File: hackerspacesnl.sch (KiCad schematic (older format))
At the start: 44 parts

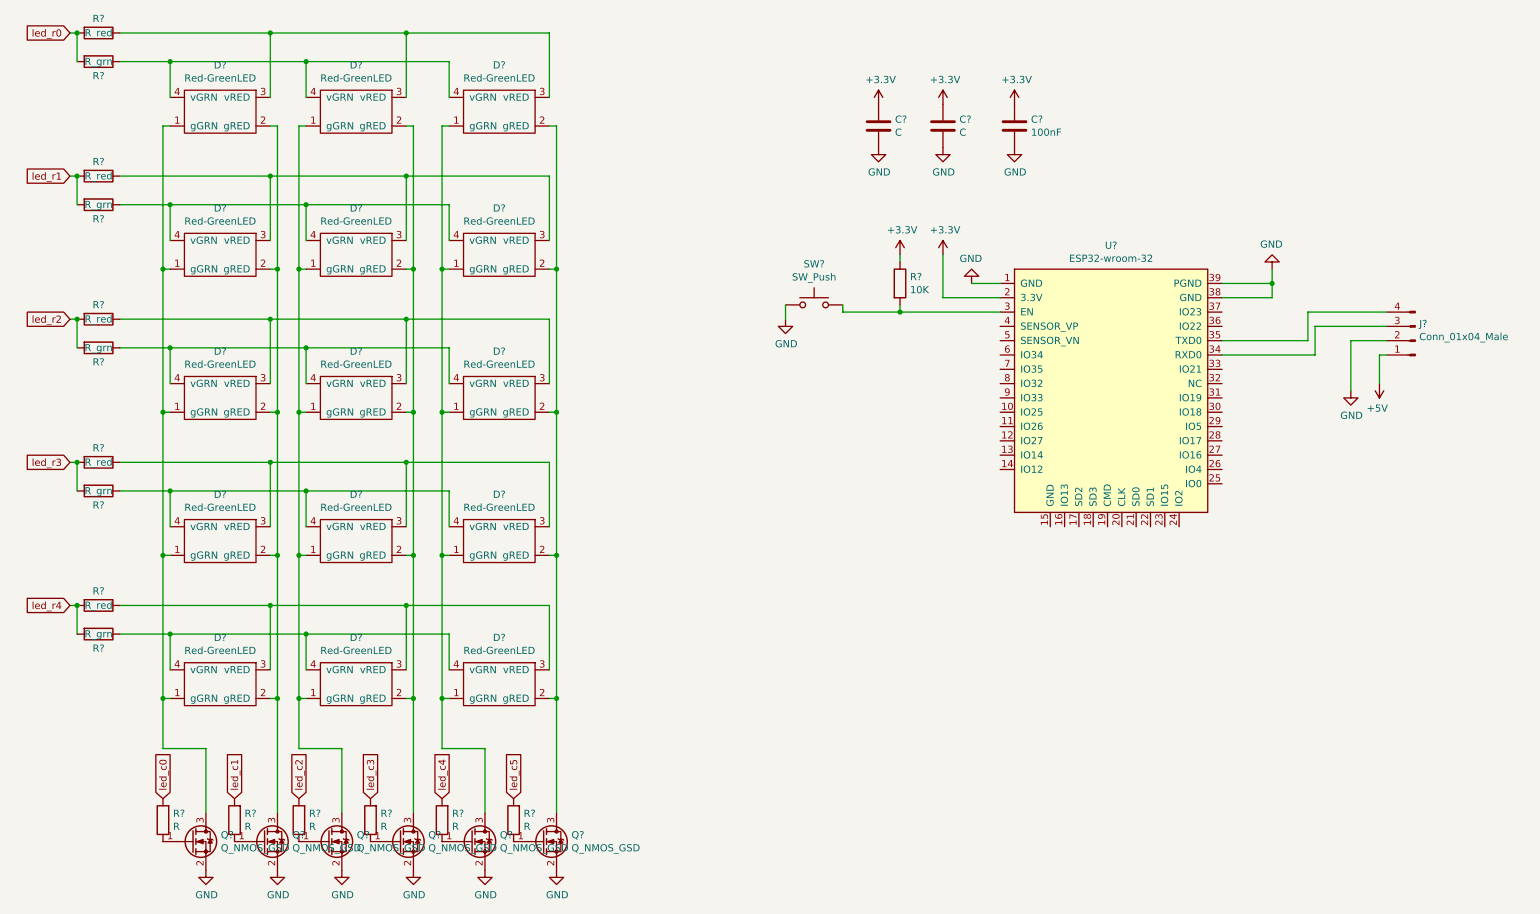
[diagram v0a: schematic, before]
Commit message: add values, connect matrix
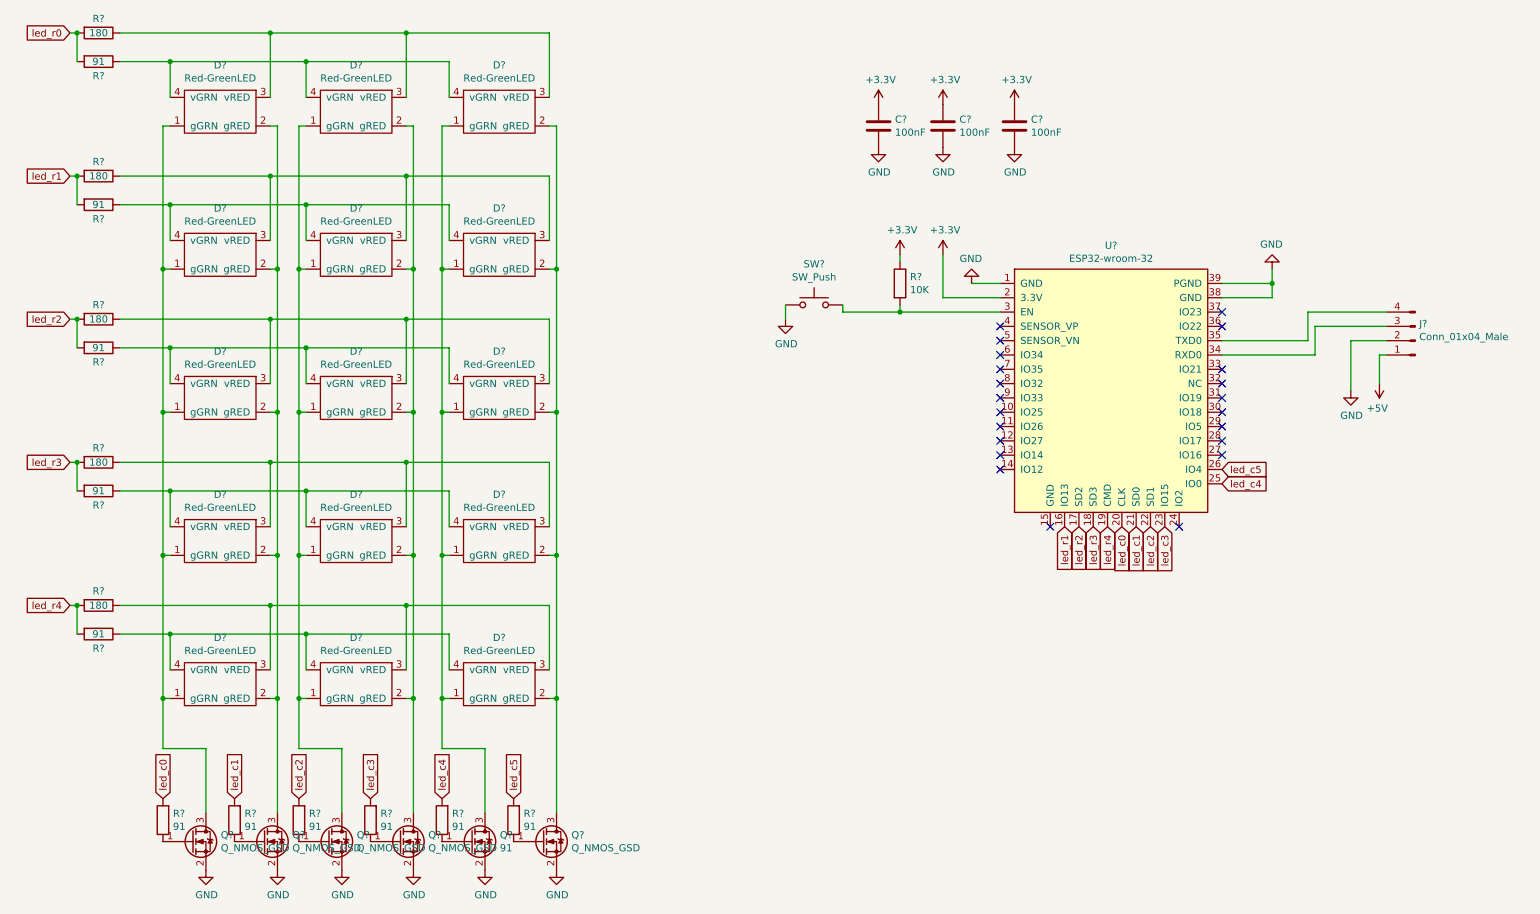
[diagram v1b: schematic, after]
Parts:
- C? (x2): value C -> 100nF
- Q?: value Q_NMOS_GSD -> 91
- R? (x5): value R_red -> 180
- R? (x5): value R_grn -> 91
- R? (x6): value R -> 91
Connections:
- net led_c0: now also U?.20 (CLK)
- net led_c1: now also U?.21 (SD0)
- net led_c2: now also U?.22 (SD1)
- net led_c3: now also U?.23 (IO15)
- net led_c4: now also U?.25 (IO0)
- net led_c5: now also U?.26 (IO4)
- net led_r1: now also U?.16 (IO13)
- net led_r2: now also U?.17 (SD2)
- net led_r3: now also U?.18 (SD3)
- net led_r4: now also U?.19 (CMD)
- no-connect marks 0 -> 22
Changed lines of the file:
@@
 P 1050 800
 F 0 "R?" V 950 800 50  0000 C CNN
-F 1 "R_red" V 1050 800 50  0000 C CNN
+F 1 "180" V 1050 800 50  0000 C CNN
 F 2 "" V 980 800 50  0001 C CNN
 F 3 "~" H 1050 800 50  0001 C CNN
@@
 P 3650 6450
 F 0 "Q?" H 3854 6496 50  0000 L CNN
-F 1 "Q_NMOS_GSD" H 3854 6405 50  0000 L CNN
+F 1 "91" H 3854 6405 50  0000 L CNN
 F 2 "" H 3850 6550 50  0001 C CNN
 F 3 "~" H 3650 6450 50  0001 C CNN
@@
 P 2000 6300
 F 0 "R?" H 1930 6254 50  0000 R CNN
-F 1 "R" H 1930 6345 50  0000 R CNN
+F 1 "91" H 1930 6345 50  0000 R CNN
 F 2 "" V 1930 6300 50  0001 C CNN
 F 3 "~" H 2000 6300 50  0001 C CNN
@@
 P 2450 6300
 F 0 "R?" H 2380 6254 50  0000 R CNN
-F 1 "R" H 2380 6345 50  0000 R CNN
+F 1 "91" H 2380 6345 50  0000 R CNN
 F 2 "" V 2380 6300 50  0001 C CNN
 F 3 "~" H 2450 6300 50  0001 C CNN
@@
 P 2950 6300
 F 0 "R?" H 2880 6254 50  0000 R CNN
-F 1 "R" H 2880 6345 50  0000 R CNN
+F 1 "91" H 2880 6345 50  0000 R CNN
 F 2 "" V 2880 6300 50  0001 C CNN
 F 3 "~" H 2950 6300 50  0001 C CNN
@@
 P 3450 6300
 F 0 "R?" H 3380 6254 50  0000 R CNN
-F 1 "R" H 3380 6345 50  0000 R CNN
+F 1 "91" H 3380 6345 50  0000 R CNN
 F 2 "" V 3380 6300 50  0001 C CNN
 F 3 "~" H 3450 6300 50  0001 C CNN
@@
 P 3950 6300
 F 0 "R?" H 3880 6254 50  0000 R CNN
-F 1 "R" H 3880 6345 50  0000 R CNN
+F 1 "91" H 3880 6345 50  0000 R CNN
 F 2 "" V 3880 6300 50  0001 C CNN
 F 3 "~" H 3950 6300 50  0001 C CNN
@@
 P 1500 6300
 F 0 "R?" H 1430 6254 50  0000 R CNN
-F 1 "R" H 1430 6345 50  0000 R CNN
+F 1 "91" H 1430 6345 50  0000 R CNN
 F 2 "" V 1430 6300 50  0001 C CNN
 F 3 "~" H 1500 6300 50  0001 C CNN
@@
 P 1050 1000
 F 0 "R?" V 1150 1000 50  0000 C CNN
-F 1 "R_grn" V 1050 1000 50  0000 C CNN
+F 1 "91" V 1050 1000 50  0000 C CNN
 F 2 "" V 980 1000 50  0001 C CNN
 F 3 "~" H 1050 1000 50  0001 C CNN
@@
 P 1050 2000
 F 0 "R?" V 1150 2000 50  0000 C CNN
-F 1 "R_grn" V 1050 2000 50  0000 C CNN
+F 1 "91" V 1050 2000 50  0000 C CNN
 F 2 "" V 980 2000 50  0001 C CNN
 F 3 "~" H 1050 2000 50  0001 C CNN
@@
 P 1050 1800
 F 0 "R?" V 950 1800 50  0000 C CNN
-F 1 "R_red" V 1050 1800 50  0000 C CNN
+F 1 "180" V 1050 1800 50  0000 C CNN
 F 2 "" V 980 1800 50  0001 C CNN
 F 3 "~" H 1050 1800 50  0001 C CNN
@@
 P 1050 3000
 F 0 "R?" V 1150 3000 50  0000 C CNN
-F 1 "R_grn" V 1050 3000 50  0000 C CNN
+F 1 "91" V 1050 3000 50  0000 C CNN
 F 2 "" V 980 3000 50  0001 C CNN
 F 3 "~" H 1050 3000 50  0001 C CNN
@@
 P 1050 2800
 F 0 "R?" V 950 2800 50  0000 C CNN
-F 1 "R_red" V 1050 2800 50  0000 C CNN
+F 1 "180" V 1050 2800 50  0000 C CNN
 F 2 "" V 980 2800 50  0001 C CNN
 F 3 "~" H 1050 2800 50  0001 C CNN
@@
 P 1050 4000
 F 0 "R?" V 1150 4000 50  0000 C CNN
-F 1 "R_grn" V 1050 4000 50  0000 C CNN
+F 1 "91" V 1050 4000 50  0000 C CNN
 F 2 "" V 980 4000 50  0001 C CNN
 F 3 "~" H 1050 4000 50  0001 C CNN
@@
 P 1050 3800
 F 0 "R?" V 950 3800 50  0000 C CNN
-F 1 "R_red" V 1050 3800 50  0000 C CNN
+F 1 "180" V 1050 3800 50  0000 C CNN
 F 2 "" V 980 3800 50  0001 C CNN
 F 3 "~" H 1050 3800 50  0001 C CNN
@@
 P 1050 5000
 F 0 "R?" V 1150 5000 50  0000 C CNN
-F 1 "R_grn" V 1050 5000 50  0000 C CNN
+F 1 "91" V 1050 5000 50  0000 C CNN
 F 2 "" V 980 5000 50  0001 C CNN
 F 3 "~" H 1050 5000 50  0001 C CNN
@@
 P 1050 4800
 F 0 "R?" V 950 4800 50  0000 C CNN
-F 1 "R_red" V 1050 4800 50  0000 C CNN
+F 1 "180" V 1050 4800 50  0000 C CNN
 F 2 "" V 980 4800 50  0001 C CNN
 F 3 "~" H 1050 4800 50  0001 C CNN
@@
 P 6500 1450
 F 0 "C?" H 6615 1496 50  0000 L CNN
-F 1 "C" H 6615 1405 50  0000 L CNN
+F 1 "100nF" H 6615 1405 50  0000 L CNN
 F 2 "" H 6538 1300 50  0001 C CNN
 F 3 "~" H 6500 1450 50  0001 C CNN
@@
 P 6950 1450
 F 0 "C?" H 7065 1496 50  0000 L CNN
-F 1 "C" H 7065 1405 50  0000 L CNN
+F 1 "100nF" H 7065 1405 50  0000 L CNN
 F 2 "" H 6988 1300 50  0001 C CNN
 F 3 "~" H 6950 1450 50  0001 C CNN
@@
 	1    0    0    -1
 $EndComp
+Text GLabel 7800 4250 3    50   Input ~ 0
+led_r1
+Text GLabel 7900 4250 3    50   Input ~ 0
+led_r2
+Text GLabel 8000 4250 3    50   Input ~ 0
+led_r3
+Text GLabel 8100 4250 3    50   Input ~ 0
+led_r4
+Text GLabel 8200 4250 3    50   Input ~ 0
+led_c0
+Text GLabel 8300 4250 3    50   Input ~ 0
+led_c1
+Text GLabel 8400 4250 3    50   Input ~ 0
+led_c2
+Text GLabel 8500 4250 3    50   Input ~ 0
+led_c3
+Text GLabel 8900 3950 2    50   Input ~ 0
+led_c4
+Text GLabel 8900 3850 2    50   Input ~ 0
+led_c5
+NoConn ~ 8600 4250
+NoConn ~ 7700 4250
+NoConn ~ 7350 3850
+NoConn ~ 7350 3750
+NoConn ~ 7350 3650
+NoConn ~ 7350 3550
+NoConn ~ 7350 3450
+NoConn ~ 7350 3350
+NoConn ~ 7350 3250
+NoConn ~ 7350 3150
+NoConn ~ 7350 3050
+NoConn ~ 7350 2950
+NoConn ~ 7350 2850
+NoConn ~ 8900 2750
+NoConn ~ 8900 2850
+NoConn ~ 8900 3150
+NoConn ~ 8900 3250
+NoConn ~ 8900 3350
+NoConn ~ 8900 3450
+NoConn ~ 8900 3550
+NoConn ~ 8900 3650
+NoConn ~ 8900 3750
 $EndSCHEMATC

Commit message: schema compleet
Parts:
- added C1: 10uF, Capacitor_SMD:C_0603_1608Metric, symbol Device:C
- added C2, C3: 100nF, Capacitor_SMD:C_0603_1608Metric, symbol Device:C
- added C6: 47uF, Capacitor_SMD:C_0805_2012Metric, symbol Device:C
- added J1: Screw_Terminal_01x02, Connector_Phoenix_MSTB:PhoenixContact_MSTBA_2,5_2-G-5,08_1x02_P5.08mm_Horizontal, symbol Connector:Screw_Terminal_01x02
- added R18: 10K, Resistor_SMD:R_0603_1608Metric, symbol Device:R
- added SW2: SW_Push, Button_Switch_SMD:SW_SPST_TL3342, symbol Switch:SW_Push
- added U1: AMS1117-3.3, Package_TO_SOT_SMD:SOT-223-3_TabPin2, symbol Regulator_Linear:AMS1117-3.3
- C4, C5: renamed from C?; footprint (none) -> Capacitor_SMD:C_0603_1608Metric
- J2: renamed from J?; footprint (none) -> Connector_PinHeader_2.54mm:PinHeader_1x04_P2.54mm_Vertical
- Q1, Q2, Q3, Q4, Q6: renamed from Q?; footprint (none) -> Package_TO_SOT_SMD:SOT-23
- Q5: renamed from Q?; value 91 -> Q_NMOS_GSD; footprint (none) -> Package_TO_SOT_SMD:SOT-23
- R1, R10, R11, R12, R13, R14, R15, R16, R2, R3, R4, R5, R6, R7, R8, R9: renamed from R?; footprint (none) -> Resistor_SMD:R_0603_1608Metric
- SW1: renamed from SW?; footprint (none) -> Button_Switch_SMD:SW_SPST_TL3342
- U2: renamed from U?; footprint (none) -> RF_Module:ESP32-WROOM-32
- gave numbers to parts that had none: 17
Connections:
- net +3V3: now also C3.1, C6.1, R18.1, U1.2 (VO)
- net +5V: now also C1.1, C2.1, J1.1 (Pin_1), U1.3 (VI)
- net GND: now also C1.2, C2.2, C3.2, C6.2, J1.2 (Pin_2), SW2.2, U1.1 (GND)
- net led_c0: now also U2.36 (IO22); no longer U2.20 (CLK)
- net led_c1: now also U2.33 (IO21); no longer U2.21 (SD0)
- net led_c2: now also U2.31 (IO19); no longer U2.22 (SD1)
- net led_c3: now also U2.30 (IO18); no longer U2.23 (IO15)
- net led_c4: now also U2.29 (IO5); no longer U2.25 (IO0)
- net led_c5: now also U2.28 (IO17); no longer U2.26 (IO4)
- net led_r1: now also U2.7 (IO35); no longer U2.16 (IO13)
- net led_r2: now also U2.8 (IO32); no longer U2.17 (SD2)
- net led_r3: now also U2.9 (IO33); no longer U2.18 (SD3)
- net led_r4: now also U2.10 (IO25); no longer U2.19 (CMD)
- new net: R18.2, SW2.1, U2.25 (IO0)
- no-connect marks 22 -> 3

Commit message: schemafoutje gefixt en eerste pcb stapjes
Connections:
- net led_r0: now also U2.14 (IO12)
- net led_r1: now also U2.16 (IO13); no longer U2.7 (IO35)
- net led_r2: now also U2.23 (IO15); no longer U2.8 (IO32)
- net led_r3: now also U2.24 (IO2); no longer U2.9 (IO33)
- net led_r4: now also U2.26 (IO4); no longer U2.10 (IO25)
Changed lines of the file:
@@
 	1    0    0    -1
 $EndComp
-Text GLabel 7150 3150 0    50   Input ~ 0
+Text GLabel 7800 4400 3    50   Input ~ 0
 led_r1
-Text GLabel 7150 3250 0    50   Input ~ 0
+Text GLabel 8500 4400 3    50   Input ~ 0
 led_r2
-Text GLabel 7150 3350 0    50   Input ~ 0
+Text GLabel 8600 4400 3    50   Input ~ 0
 led_r3
-Text GLabel 7150 3450 0    50   Input ~ 0
+Text GLabel 9100 3850 2    50   Input ~ 0
 led_r4
 Text GLabel 9100 2850 2    50   Input ~ 0
@@
 	9600 3500 9600 3550
 Wire Wire Line
-	7150 3150 7350 3150
-Wire Wire Line
-	7350 3250 7150 3250
-Wire Wire Line
-	7150 3350 7350 3350
-Wire Wire Line
-	7350 3450 7150 3450
-Wire Wire Line
 	9100 2850 8900 2850
 Wire Wire Line
@@
 Wire Wire Line
 	8900 3650 9100 3650
+Wire Wire Line
+	9100 3850 8900 3850
+Wire Wire Line
+	8600 4400 8600 4250
+Wire Wire Line
+	8500 4400 8500 4250
+Wire Wire Line
+	7800 4400 7800 4250
+Text GLabel 7200 3850 0    50   Input ~ 0
+led_r0
+Wire Wire Line
+	7200 3850 7350 3850
 $EndSCHEMATC

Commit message: led footprint
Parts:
- D1, D10, D11, D12, D13, D14, D15, D2, D3, D4, D5, D6, D7, D8, D9: footprint (none) -> hsnl:LED_0805_multicolor
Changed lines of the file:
@@
 F 0 "D1" V 1575 1350 50  0000 C CNN
 F 1 "Red-GreenLED" V 1666 1350 50  0000 C CNN
-F 2 "" V 1550 1500 50  0001 C CNN
+F 2 "hsnl:LED_0805_multicolor" V 1550 1500 50  0001 C CNN
 F 3 "" V 1550 1500 50  0001 C CNN
 	1    1900 1350
@@
 F 0 "D2" V 1575 2350 50  0000 C CNN
 F 1 "Red-GreenLED" V 1666 2350 50  0000 C CNN
-F 2 "" V 1550 2500 50  0001 C CNN
+F 2 "hsnl:LED_0805_multicolor" V 1550 2500 50  0001 C CNN
 F 3 "" V 1550 2500 50  0001 C CNN
 	1    1900 2350
@@
 F 0 "D3" V 1575 3350 50  0000 C CNN
 F 1 "Red-GreenLED" V 1666 3350 50  0000 C CNN
-F 2 "" V 1550 3500 50  0001 C CNN
+F 2 "hsnl:LED_0805_multicolor" V 1550 3500 50  0001 C CNN
 F 3 "" V 1550 3500 50  0001 C CNN
 	1    1900 3350
@@
 F 0 "D6" V 2525 1350 50  0000 C CNN
 F 1 "Red-GreenLED" V 2616 1350 50  0000 C CNN
-F 2 "" V 2500 1500 50  0001 C CNN
+F 2 "hsnl:LED_0805_multicolor" V 2500 1500 50  0001 C CNN
 F 3 "" V 2500 1500 50  0001 C CNN
 	1    2850 1350
@@
 F 0 "D7" V 2525 2350 50  0000 C CNN
 F 1 "Red-GreenLED" V 2616 2350 50  0000 C CNN
-F 2 "" V 2500 2500 50  0001 C CNN
+F 2 "hsnl:LED_0805_multicolor" V 2500 2500 50  0001 C CNN
 F 3 "" V 2500 2500 50  0001 C CNN
 	1    2850 2350
@@
 F 0 "D8" V 2525 3350 50  0000 C CNN
 F 1 "Red-GreenLED" V 2616 3350 50  0000 C CNN
-F 2 "" V 2500 3500 50  0001 C CNN
+F 2 "hsnl:LED_0805_multicolor" V 2500 3500 50  0001 C CNN
 F 3 "" V 2500 3500 50  0001 C CNN
 	1    2850 3350
@@
 F 0 "D11" V 3525 1350 50  0000 C CNN
 F 1 "Red-GreenLED" V 3616 1350 50  0000 C CNN
-F 2 "" V 3500 1500 50  0001 C CNN
+F 2 "hsnl:LED_0805_multicolor" V 3500 1500 50  0001 C CNN
 F 3 "" V 3500 1500 50  0001 C CNN
 	1    3850 1350
@@
 F 0 "D12" V 3525 2350 50  0000 C CNN
 F 1 "Red-GreenLED" V 3616 2350 50  0000 C CNN
-F 2 "" V 3500 2500 50  0001 C CNN
+F 2 "hsnl:LED_0805_multicolor" V 3500 2500 50  0001 C CNN
 F 3 "" V 3500 2500 50  0001 C CNN
 	1    3850 2350
@@
 F 0 "D13" V 3525 3350 50  0000 C CNN
 F 1 "Red-GreenLED" V 3616 3350 50  0000 C CNN
-F 2 "" V 3500 3500 50  0001 C CNN
+F 2 "hsnl:LED_0805_multicolor" V 3500 3500 50  0001 C CNN
 F 3 "" V 3500 3500 50  0001 C CNN
 	1    3850 3350
@@
 F 0 "D4" V 1575 4350 50  0000 C CNN
 F 1 "Red-GreenLED" V 1666 4350 50  0000 C CNN
-F 2 "" V 1550 4500 50  0001 C CNN
+F 2 "hsnl:LED_0805_multicolor" V 1550 4500 50  0001 C CNN
 F 3 "" V 1550 4500 50  0001 C CNN
 	1    1900 4350
@@
 F 0 "D9" V 2525 4350 50  0000 C CNN
 F 1 "Red-GreenLED" V 2616 4350 50  0000 C CNN
-F 2 "" V 2500 4500 50  0001 C CNN
+F 2 "hsnl:LED_0805_multicolor" V 2500 4500 50  0001 C CNN
 F 3 "" V 2500 4500 50  0001 C CNN
 	1    2850 4350
@@
 F 0 "D14" V 3525 4350 50  0000 C CNN
 F 1 "Red-GreenLED" V 3616 4350 50  0000 C CNN
-F 2 "" V 3500 4500 50  0001 C CNN
+F 2 "hsnl:LED_0805_multicolor" V 3500 4500 50  0001 C CNN
 F 3 "" V 3500 4500 50  0001 C CNN
 	1    3850 4350
@@
 F 0 "D10" V 2525 5350 50  0000 C CNN
 F 1 "Red-GreenLED" V 2616 5350 50  0000 C CNN
-F 2 "" V 2500 5500 50  0001 C CNN
+F 2 "hsnl:LED_0805_multicolor" V 2500 5500 50  0001 C CNN
 F 3 "" V 2500 5500 50  0001 C CNN
 	1    2850 5350
@@
 F 0 "D15" V 3525 5350 50  0000 C CNN
 F 1 "Red-GreenLED" V 3616 5350 50  0000 C CNN
-F 2 "" V 3500 5500 50  0001 C CNN
+F 2 "hsnl:LED_0805_multicolor" V 3500 5500 50  0001 C CNN
 F 3 "" V 3500 5500 50  0001 C CNN
 	1    3850 5350
@@
 F 0 "D5" V 1575 5350 50  0000 C CNN
 F 1 "Red-GreenLED" V 1666 5350 50  0000 C CNN
-F 2 "" V 1550 5500 50  0001 C CNN
+F 2 "hsnl:LED_0805_multicolor" V 1550 5500 50  0001 C CNN
 F 3 "" V 1550 5500 50  0001 C CNN
 	1    1900 5350

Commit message: fixed LED symbol, began initial layout
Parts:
- D4: value Red-GreenLED -> Red-GreenLED-parts
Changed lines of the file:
@@
 P 1900 4350
 F 0 "D4" V 1575 4350 50  0000 C CNN
-F 1 "Red-GreenLED" V 1666 4350 50  0000 C CNN
+F 1 "Red-GreenLED-parts" V 1666 4350 50  0000 C CNN
 F 2 "hsnl:LED_0805_multicolor" V 1550 4500 50  0001 C CNN
 F 3 "" V 1550 4500 50  0001 C CNN

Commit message: sorted ratsnest, removed map as we will go bigger
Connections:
- wire segments 192 -> 188
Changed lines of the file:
@@
 	3500 1450 3450 1450
 Wire Wire Line
-	3450 1450 3450 2450
-Wire Wire Line
 	3450 2450 3500 2450
 Wire Wire Line
 	4200 2450 4250 2450
-Wire Wire Line
-	4250 2450 4250 1450
 Wire Wire Line
 	4250 1450 4200 1450
@@
 Wire Wire Line
 	3450 5450 3450 4450
-Connection ~ 3450 2450
 Wire Wire Line
 	3500 3450 3450 3450
@@
 Wire Wire Line
 	4250 5450 4250 4450
-Connection ~ 4250 2450
 Wire Wire Line
 	4200 3450 4250 3450
@@
 Connection ~ 2500 2000
 Wire Wire Line
-	4200 1250 4200 800
-Wire Wire Line
 	1200 800  2250 800
 Wire Wire Line
@@
 Wire Wire Line
 	2500 1000 3500 1000
-Wire Wire Line
-	3500 1000 3500 1250
 Connection ~ 2500 1000
 Wire Wire Line
